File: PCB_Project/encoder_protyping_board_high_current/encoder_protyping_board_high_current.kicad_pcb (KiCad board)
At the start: 2 copper layers, 0 parts

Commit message: high current version done
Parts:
- added 1.2K: 1.2k, Resistor_SMD:R_0402_1005Metric, F.Cu at (188.0, 109.4)
- added 1.6K: 1.6k, Resistor_SMD:R_0402_1005Metric, F.Cu at (188.0, 111.4)
- added 1.6K: 1.6k, Resistor_SMD:R_0402_1005Metric, F.Cu at (188.0, 110.4)
- added 10nF: 0.01 μF, Capacitor_SMD:C_0402_1005Metric, F.Cu at (190.8, 100.0)
- added 4.7µF: 4.7 μF, Capacitor_SMD:C_0402_1005Metric, F.Cu at (189.8, 100.0)
- added 4.7µF: 4.7 μF, Capacitor_THT:CP_Radial_D5.0mm_P2.00mm, F.Cu at (198.8, 115.8)
- added 4.7µF: 4.7 μF, Capacitor_THT:CP_Radial_D5.0mm_P2.00mm, F.Cu at (198.6, 98.5)
- added A3909: ~, my trash:SSOP-10_3.9x4.9mm_P1.00mm, F.Cu at (199.8, 104.4)
- added A3909: ~, my trash:SSOP-10_3.9x4.9mm_P1.00mm, F.Cu at (199.8, 109.9)
- added J1: Conn_01x08, Connector_PinSocket_2.54mm:PinSocket_1x08_P2.54mm_Vertical, F.Cu at (206.8, 97.2)
- added J2: Conn_01x02_Pin, Connector_PinHeader_2.54mm:PinHeader_1x02_P2.54mm_Vertical, F.Cu at (186.7, 114.2)
- added J3: Conn_01x04_Pin, Connector_PinSocket_2.54mm:PinSocket_1x04_P2.54mm_Vertical, F.Cu at (186.6, 97.1)
- added JP1: SolderJumper_3_Open, Jumper:SolderJumper-3_P1.3mm_Open_RoundedPad1.0x1.5mm_NumberLabels, B.Cu at (193.9, 115.5)
- added JP2: SolderJumper_3_Open, Jumper:SolderJumper-3_P1.3mm_Open_RoundedPad1.0x1.5mm_NumberLabels, B.Cu at (191.4, 115.5)
- added PCA9629A: ~, Package_SO:TSSOP-16_4.4x5mm_P0.65mm, F.Cu at (191.0, 103.9)
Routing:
- net GND: track 0.00 -> 59.9 mm, vias 0 -> 14
- net +5V: track 0.00 -> 58.0 mm, vias 0 -> 3
- net +12V: track 0.00 -> 31.1 mm, vias 0 -> 2
- net Net-(J1-Pin_6): track 0.00 -> 30.5 mm
- net Net-(J1-Pin_7): track 0.00 -> 30.4 mm
- net I2C_SDA: track 0.00 -> 28.6 mm
- net I2C_SCL: track 0.00 -> 23.4 mm, vias 0 -> 2
- net Net-(JP2-C): track 0.00 -> 18.8 mm, vias 0 -> 3
- net Net-(JP1-C): track 0.00 -> 17.6 mm, vias 0 -> 3
- net Net-(J1-Pin_1): track 0.00 -> 14.2 mm
- net Net-(J1-Pin_3): track 0.00 -> 14.1 mm
- net Net-(U1-OUT0): track 0.00 -> 10.4 mm
- net Net-(U1-OUT2): track 0.00 -> 10.1 mm
- net Net-(J1-Pin_4): track 0.00 -> 9.32 mm
- net Net-(J1-Pin_2): track 0.00 -> 9.08 mm
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- added copper zone on B.Cu, net GND
- added copper zone on F.Cu, net GND
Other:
- board outline added: 23.8 x 23.5 mm
- board text added: "I2C Stepper Driver-E 1.5 Amp coil limit D Verbeek STARR 2024"
- board text added: "↑↑ 0x58 ↑↓ 0x5A ↓↑ 0x5C ↓↓ 0x5E"

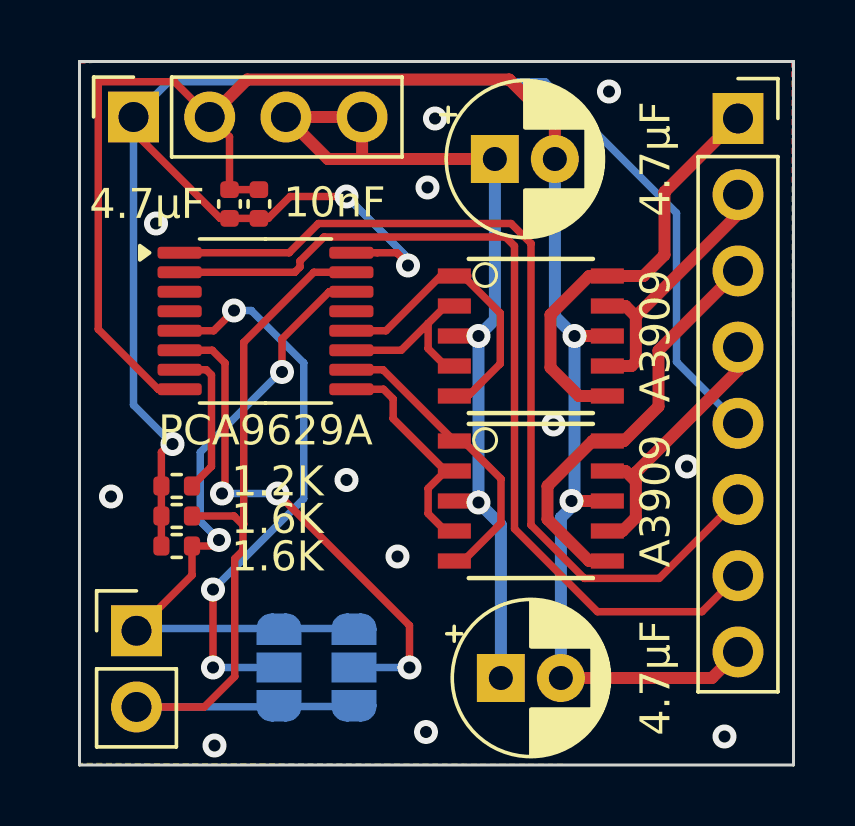
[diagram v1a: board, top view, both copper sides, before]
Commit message: auto clean up on the board
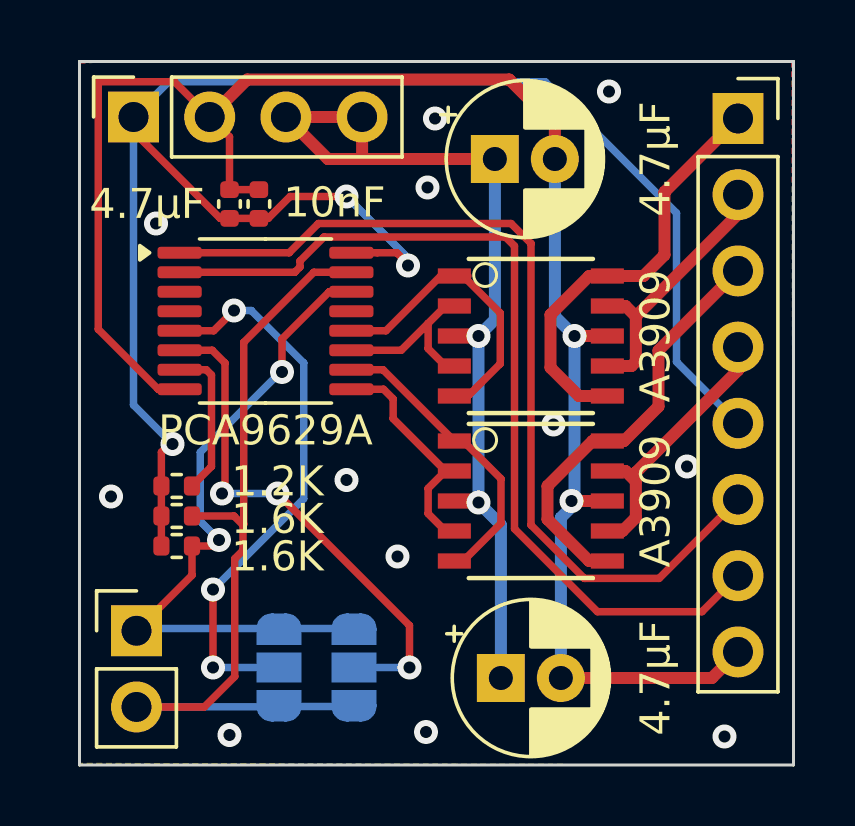
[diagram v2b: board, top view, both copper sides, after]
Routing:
- net Net-(U1-OUT2): track 10.1 -> 9.46 mm
- net Net-(U1-OUT3): track 7.72 -> 7.13 mm
- net Net-(U1-OUT1): track 6.00 -> 5.41 mm
- net +5V: track 58.0 -> 57.4 mm

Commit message: pin headers not pin sockets
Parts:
- J1: footprint Connector_PinSocket_2.54mm:PinSocket_1x08_P2.54mm_Vertical -> Connector_PinHeader_2.54mm:PinHeader_1x08_P2.54mm_Vertical
- J3: footprint Connector_PinSocket_2.54mm:PinSocket_1x04_P2.54mm_Vertical -> Connector_PinHeader_2.54mm:PinHeader_1x04_P2.54mm_Vertical
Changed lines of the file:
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@@
 		)
 	)
-	(footprint "Connector_PinSocket_2.54mm:PinSocket_1x04_P2.54mm_Vertical"
+	(footprint "Connector_PinHeader_2.54mm:PinHeader_1x04_P2.54mm_Vertical"
 		(layer "F.Cu")
 		(at 186.6 97.1 90)
-		(descr "Through hole straight socket strip, 1x04, 2.54mm pitch, single row (from Kicad 4.0.7), script generated")
-		(tags "Through hole socket strip THT 1x04 2.54mm single row")
+		(descr "Through hole straight pin header, 1x04, 2.54mm pitch, single row")
+		(tags "Through hole pin header THT 1x04 2.54mm single row")
 		(property "Reference" "J3"
-			(at 0 -2.77 -90)
+			(at 0 -2.33 90)
 			(layer "F.SilkS")
 			(hide yes)
@@
 		)
 		(property "Value" "Conn_01x04_Pin"
-			(at 0 10.39 -90)
+			(at 0 9.95 90)
 			(layer "F.Fab")
 			(effects
@@
 			)
 		)
-		(property ki_fp_filters "Connector*:*_1x??_*")
-		(sheetname "Root")
-		(sheetfile "encoder_protyping_board_high_current.kicad_sch")
 		(attr through_hole)
 		(fp_line
-			(start 1.33 -1.33)
-			(end 1.33 0)
-			(stroke
-				(width 0.12)
-				(type solid)
-			)
-			(layer "F.SilkS")
-		)
-		(fp_line
-			(start 0 -1.33)
-			(end 1.33 -1.33)
+			(start -1.33 -1.33)
+			(end 0 -1.33)
+			(stroke
+				(width 0.12)
+				(type solid)
+			)
+			(layer "F.SilkS")
+		)
+		(fp_line
+			(start -1.33 0)
+			(end -1.33 -1.33)
 			(stroke
 				(width 0.12)
@@
 		)
 		(fp_line
-			(start 1.75 -1.8)
-			(end 1.75 9.4)
+			(start 1.8 -1.8)
+			(end -1.8 -1.8)
 			(stroke
 				(width 0.05)
@@
 		(fp_line
 			(start -1.8 -1.8)
-			(end 1.75 -1.8)
-			(stroke
-				(width 0.05)
-				(type solid)
-			)
-			(layer "F.CrtYd")
-		)
-		(fp_line
-			(start 1.75 9.4)
 			(end -1.8 9.4)
 			(stroke
@@
 		)
 		(fp_line
+			(start 1.8 9.4)
+			(end 1.8 -1.8)
+			(stroke
+				(width 0.05)
+				(type solid)
+			)
+			(layer "F.CrtYd")
+		)
+		(fp_line
 			(start -1.8 9.4)
-			(end -1.8 -1.8)
-			(stroke
-				(width 0.05)
-				(type solid)
-			)
-			(layer "F.CrtYd")
-		)
-		(fp_line
-			(start 0.635 -1.27)
-			(end 1.27 -0.635)
-			(stroke
-				(width 0.1)
-				(type solid)
-			)
-			(layer "F.Fab")
-		)
-		(fp_line
-			(start -1.27 -1.27)
-			(end 0.635 -1.27)
-			(stroke
-				(width 0.1)
-				(type solid)
-			)
-			(layer "F.Fab")
-		)
-		(fp_line
-			(start 1.27 -0.635)
+			(end 1.8 9.4)
+			(stroke
+				(width 0.05)
+				(type solid)
+			)
+			(layer "F.CrtYd")
+		)
+		(fp_line
+			(start 1.27 -1.27)
 			(end 1.27 8.89)
+			(stroke
+				(width 0.1)
+				(type solid)
+			)
+			(layer "F.Fab")
+		)
+		(fp_line
+			(start -0.635 -1.27)
+			(end 1.27 -1.27)
+			(stroke
+				(width 0.1)
+				(type solid)
+			)
+			(layer "F.Fab")
+		)
+		(fp_line
+			(start -1.27 -0.635)
+			(end -0.635 -1.27)
 			(stroke
 				(width 0.1)
@@
 		(fp_line
 			(start -1.27 8.89)
-			(end -1.27 -1.27)
+			(end -1.27 -0.635)
 			(stroke
 				(width 0.1)
@@
 		)
 		(fp_text user "${REFERENCE}"
-			(at 0 3.81 0)
+			(at 0 3.81 180)
 			(layer "F.Fab")
 			(effects
@@
 			(pintype "passive")
 		)
-		(model "${KICAD8_3DMODEL_DIR}/Connector_PinSocket_2.54mm.3dshapes/PinSocket_1x04_P2.54mm_Vertical.wrl"
+		(model "${KICAD8_3DMODEL_DIR}/Connector_PinHeader_2.54mm.3dshapes/PinHeader_1x04_P2.54mm_Vertical.wrl"
 			(offset
 				(xyz 0 0 0)
@@
 		)
 	)
-	(footprint "Connector_PinSocket_2.54mm:PinSocket_1x08_P2.54mm_Vertical"
+	(footprint "Connector_PinHeader_2.54mm:PinHeader_1x08_P2.54mm_Vertical"
 		(layer "F.Cu")
 		(at 206.75 97.15)
-		(descr "Through hole straight socket strip, 1x08, 2.54mm pitch, single row (from Kicad 4.0.7), script generated")
-		(tags "Through hole socket strip THT 1x08 2.54mm single row")
+		(descr "Through hole straight pin header, 1x08, 2.54mm pitch, single row")
+		(tags "Through hole pin header THT 1x08 2.54mm single row")
 		(property "Reference" "J1"
-			(at 0 -2.77 0)
+			(at 0 -2.33 0)
 			(layer "F.SilkS")
 			(hide yes)
@@
 		)
 		(property "Value" "Conn_01x08"
-			(at 0 20.55 0)
+			(at 0 20.11 0)
 			(layer "F.Fab")
 			(effects
@@
 			)
 		)
-		(property ki_fp_filters "Connector*:*_1x??_*")
-		(sheetname "Root")
-		(sheetfile "encoder_protyping_board_high_current.kicad_sch")
 		(attr through_hole)
+		(fp_line
+			(start -1.33 -1.33)
+			(end 0 -1.33)
+			(stroke
+				(width 0.12)
+				(type solid)
+			)
+			(layer "F.SilkS")
+		)
+		(fp_line
+			(start -1.33 0)
+			(end -1.33 -1.33)
+			(stroke
+				(width 0.12)
+				(type solid)
+			)
+			(layer "F.SilkS")
+		)
 		(fp_line
 			(start -1.33 1.27)
@@
 		)
 		(fp_line
-			(start 0 -1.33)
-			(end 1.33 -1.33)
-			(stroke
-				(width 0.12)
-				(type solid)
-			)
-			(layer "F.SilkS")
-		)
-		(fp_line
-			(start 1.33 -1.33)
-			(end 1.33 0)
-			(stroke
-				(width 0.12)
-				(type solid)
-			)
-			(layer "F.SilkS")
-		)
-		(fp_line
 			(start 1.33 1.27)
 			(end 1.33 19.11)
@@
 		(fp_line
 			(start -1.8 -1.8)
-			(end 1.75 -1.8)
+			(end -1.8 19.55)
 			(stroke
 				(width 0.05)
@@
 		(fp_line
 			(start -1.8 19.55)
+			(end 1.8 19.55)
+			(stroke
+				(width 0.05)
+				(type solid)
+			)
+			(layer "F.CrtYd")
+		)
+		(fp_line
+			(start 1.8 -1.8)
 			(end -1.8 -1.8)
 			(stroke
@@
 		)
 		(fp_line
-			(start 1.75 -1.8)
-			(end 1.75 19.55)
-			(stroke
-				(width 0.05)
-				(type solid)
-			)
-			(layer "F.CrtYd")
-		)
-		(fp_line
-			(start 1.75 19.55)
-			(end -1.8 19.55)
-			(stroke
-				(width 0.05)
-				(type solid)
-			)
-			(layer "F.CrtYd")
-		)
-		(fp_line
-			(start -1.27 -1.27)
-			(end 0.635 -1.27)
+			(start 1.8 19.55)
+			(end 1.8 -1.8)
+			(stroke
+				(width 0.05)
+				(type solid)
+			)
+			(layer "F.CrtYd")
+		)
+		(fp_line
+			(start -1.27 -0.635)
+			(end -0.635 -1.27)
 			(stroke
 				(width 0.1)
@@
 		(fp_line
 			(start -1.27 19.05)
-			(end -1.27 -1.27)
-			(stroke
-				(width 0.1)
-				(type solid)
-			)
-			(layer "F.Fab")
-		)
-		(fp_line
-			(start 0.635 -1.27)
-			(end 1.27 -0.635)
-			(stroke
-				(width 0.1)
-				(type solid)
-			)
-			(layer "F.Fab")
-		)
-		(fp_line
-			(start 1.27 -0.635)
+			(end -1.27 -0.635)
+			(stroke
+				(width 0.1)
+				(type solid)
+			)
+			(layer "F.Fab")
+		)
+		(fp_line
+			(start -0.635 -1.27)
+			(end 1.27 -1.27)
+			(stroke
+				(width 0.1)
+				(type solid)
+			)
+			(layer "F.Fab")
+		)
+		(fp_line
+			(start 1.27 -1.27)
 			(end 1.27 19.05)
 			(stroke
@@
 			(pintype "passive")
 		)
-		(model "${KICAD8_3DMODEL_DIR}/Connector_PinSocket_2.54mm.3dshapes/PinSocket_1x08_P2.54mm_Vertical.wrl"
+		(model "${KICAD8_3DMODEL_DIR}/Connector_PinHeader_2.54mm.3dshapes/PinHeader_1x08_P2.54mm_Vertical.wrl"
 			(offset
 				(xyz 0 0 0)
@@
 		)
 		(fp_circle
-			(center -1.524 -2.032)
-			(end -1.905 -2.032)
+			(center -1.397 -2.032)
+			(end -1.778 -2.032)
 			(stroke
 				(width 0.1)
@@
 		)
 		(fp_circle
-			(center -1.524 -2.032)
-			(end -1.905 -2.032)
-			(stroke
-				(width 0.1)
+			(center -1.397 -2.032)
+			(end -1.778 -2.032)
+			(stroke
+				(width 0.1)

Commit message: finaly did that change to make it so this board could run with just a single chip
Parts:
- U2, U3: renamed from A3909; footprint my trash:SSOP-10_3.9x4.9mm_P1.00mm -> Package_SO:SSOP-10_3.9x4.9mm_P1.00mm
- renumbered 4.7µF to C1, 10nF to C2, 4.7µF to C3, 4.7µF to C4, J2 to J1, J3 to J2, J1 to J3, JP2 to JP1, JP1 to JP2, 1.6K to R1, 1.6K to R2, 1.2K to R3, PCA9629A to U1
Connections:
- J3 pad 1: Net-(J1-Pin_1) -> Net-(J3-Pin_1)
- J3 pad 2: Net-(J1-Pin_2) -> Net-(J3-Pin_2)
- J3 pad 3: Net-(J1-Pin_3) -> Net-(J3-Pin_3)
- J3 pad 4: Net-(J1-Pin_4) -> Net-(J3-Pin_4)
- U2 pad 10: Net-(J1-Pin_1) -> Net-(J3-Pin_1)
- U2 pad 6: Net-(J1-Pin_1) -> Net-(J3-Pin_4)
- U2 pad 7: Net-(J1-Pin_2) -> Net-(J3-Pin_3)
- U2 pad 9: Net-(J1-Pin_2) -> Net-(J3-Pin_2)
- U3 pad 10: Net-(J1-Pin_3) -> Net-(J3-Pin_1)
- U3 pad 6: Net-(J1-Pin_3) -> Net-(J3-Pin_4)
- U3 pad 7: Net-(J1-Pin_4) -> Net-(J3-Pin_3)
- U3 pad 9: Net-(J1-Pin_4) -> Net-(J3-Pin_2)
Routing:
- net Net-(J3-Pin_1): track 0.00 -> 14.7 mm
- net Net-(J3-Pin_2): track 0.00 -> 14.4 mm, vias 0 -> 2
- net Net-(J1-Pin_1): track 14.2 -> 0.00 mm
- net Net-(J1-Pin_3): track 14.1 -> 0.00 mm
- net Net-(J3-Pin_3): track 0.00 -> 13.5 mm, vias 0 -> 2
- net Net-(J3-Pin_4): track 0.00 -> 12.2 mm
- net Net-(J1-Pin_4): track 9.32 -> 0.00 mm
- net Net-(J1-Pin_2): track 9.08 -> 0.00 mm
- net GND: vias 14 -> 12

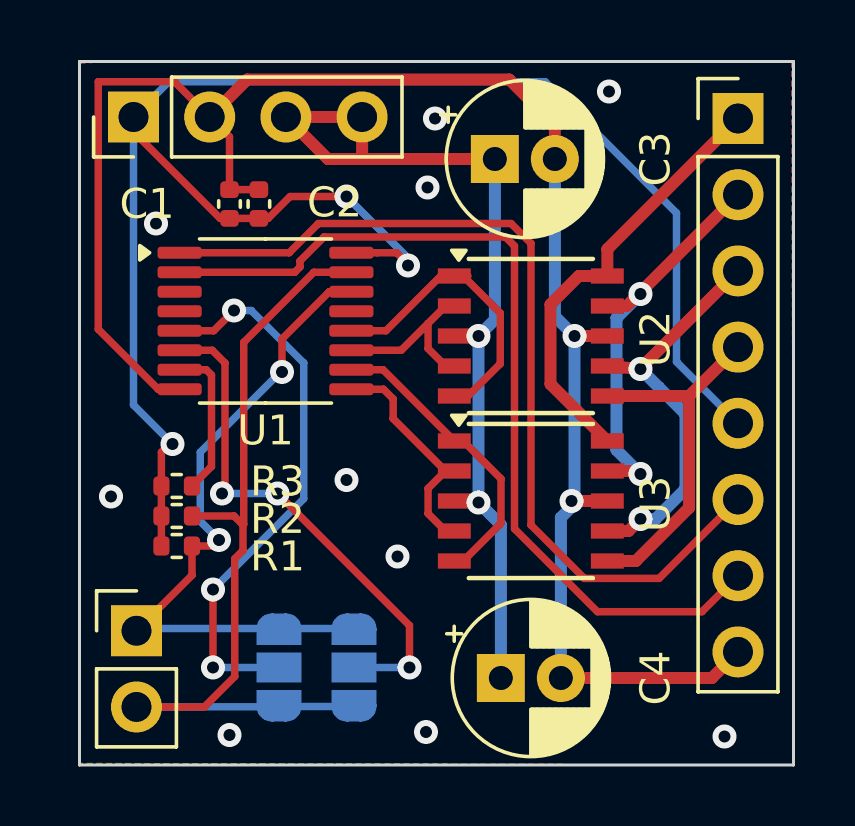
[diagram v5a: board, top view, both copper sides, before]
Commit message: that would have been bad
changed the outputs to the chips but not the inputs
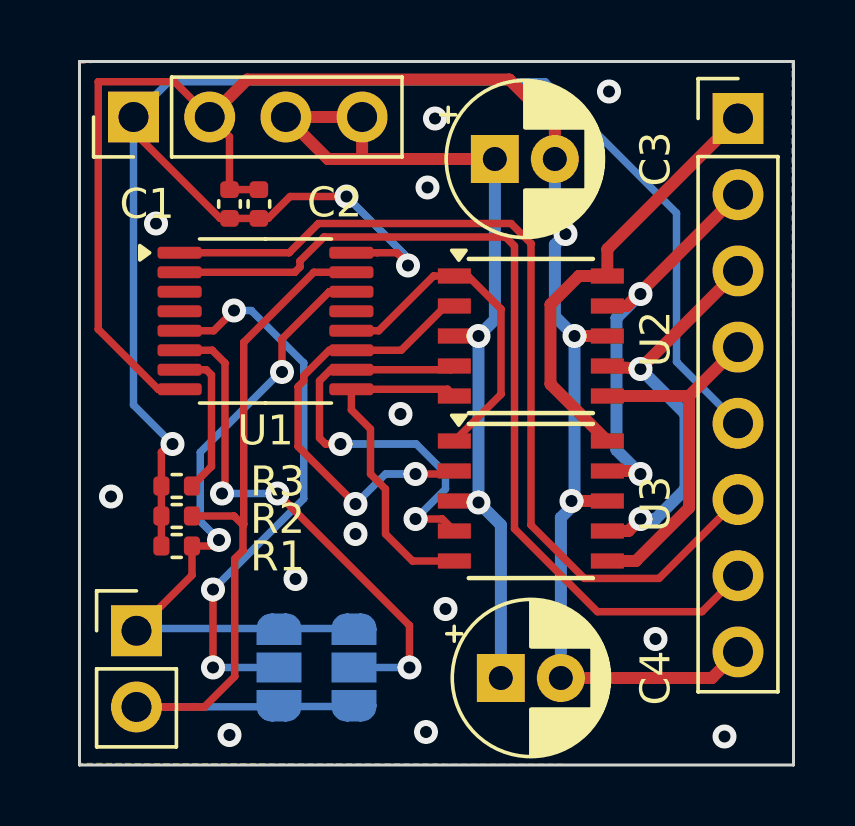
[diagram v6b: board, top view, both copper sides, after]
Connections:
- U2 pad 4: Net-(U1-OUT1) -> Net-(U1-OUT2)
- U2 pad 5: Net-(U1-OUT0) -> Net-(U1-OUT3)
- U3 pad 1: Net-(U1-OUT2) -> Net-(U1-OUT0)
- U3 pad 2: Net-(U1-OUT3) -> Net-(U1-OUT1)
- U3 pad 4: Net-(U1-OUT3) -> Net-(U1-OUT2)
- U3 pad 5: Net-(U1-OUT2) -> Net-(U1-OUT3)
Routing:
- net Net-(U1-OUT1): track 5.41 -> 14.8 mm, vias 0 -> 2
- net Net-(U1-OUT2): track 9.46 -> 14.7 mm, vias 0 -> 2
- net Net-(U1-OUT3): track 7.13 -> 11.5 mm
- net Net-(U1-OUT0): track 10.1 -> 11.2 mm
- net Net-(J3-Pin_2): track 14.4 -> 13.7 mm
- net GND: track 59.8 -> 60.1 mm, vias 12 -> 16
